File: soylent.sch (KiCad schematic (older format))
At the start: 21 parts, among them J1 DB9_Female, J2 Conn_01x04, J3 Conn_01x04, J4 Conn_02x03_Counter_Clockwise, Q1 BC847BPN, Q2 BC847BPN, U1 ATtiny202-SS, U2 MIC5504-3.3YM5

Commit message: Swap analog lines and reroute
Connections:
- net PA1: now also Q2.1 (E1), Q2.4 (E2), R5.1, R6.2
- net PA2: now also J4.1 (Pin_1); no longer Q2.1 (E1), Q2.4 (E2), R5.1, R6.2
- no-connect marks 8 -> 7
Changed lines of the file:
@@
 UPDI
-$Comp
-L Connector_Generic:Conn_02x03_Counter_Clockwise J4
-U 1 1 5DDE85A2
-P 6250 2800
-F 0 "J4" H 6300 3025 50  0000 C CNN
-F 1 "Conn_02x03_Counter_Clockwise" V 6345 2980 50  0001 L CNN
-F 2 "Pin_Headers:Pin_Header_Straight_2x03_Pitch2.54mm" H 6250 2800 50  0001 C CNN
-F 3 "~" H 6250 2800 50  0001 C CNN
-	1    6250 2800
-	1    0    0    1
-$EndComp
 $Comp
 L Transistor_BJT:BC847BPN Q1
@@
 	8250 4250 8250 2400
 Wire Wire Line
-	4000 3700 4400 3700
-Wire Wire Line
-	4400 3700 4400 3000
-Wire Wire Line
 	4400 3000 4600 3000
-Connection ~ 4000 3700
-NoConn ~ 6050 2900
 NoConn ~ 6050 2700
 NoConn ~ 6550 2700
 NoConn ~ 6550 2800
+$Comp
+L Connector_Generic:Conn_02x03_Counter_Clockwise J4
+U 1 1 5DDE85A2
+P 6250 2800
+F 0 "J4" H 6300 3025 50  0000 C CNN
+F 1 "Conn_02x03_Counter_Clockwise" V 6345 2980 50  0001 L CNN
+F 2 "Pin_Headers:Pin_Header_Straight_2x03_Pitch2.54mm" H 6250 2800 50  0001 C CNN
+F 3 "~" H 6250 2800 50  0001 C CNN
+	1    6250 2800
+	1    0    0    1
+$EndComp
+Wire Wire Line
+	3950 3600 4400 3600
+Connection ~ 3950 3600
+Wire Wire Line
+	4400 3600 4400 3000
+Wire Wire Line
+	4000 3700 6050 3700
+Wire Wire Line
+	6050 2900 6050 3700
+Connection ~ 4000 3700
 $EndSCHEMATC

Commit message: Insert a resistor on output
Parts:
- added R8: 100R, Resistors_SMD:R_0603_HandSoldering, symbol Device:R
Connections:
- net PA2: now also R8.2; no longer J4.1 (Pin_1)
- new net: J4.1 (Pin_1), R8.1
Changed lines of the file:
@@
 	4400 3600 4400 3000
 Wire Wire Line
-	4000 3700 6050 3700
+	4000 3700 5400 3700
 Wire Wire Line
 	6050 2900 6050 3700
 Connection ~ 4000 3700
+$Comp
+L Device:R R8
+U 1 1 5DFD8224
+P 5550 3700
+F 0 "R8" V 5343 3700 50  0000 C CNN
+F 1 "100R" V 5434 3700 50  0000 C CNN
+F 2 "Resistors_SMD:R_0603_HandSoldering" V 5480 3700 50  0001 C CNN
+F 3 "~" H 5550 3700 50  0001 C CNN
+	1    5550 3700
+	0    1    1    0
+$EndComp
+Wire Wire Line
+	5700 3700 6050 3700
 $EndSCHEMATC

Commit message: Switch to an RC filter
    http://sim.okawa-denshi.jp/en/CRtool.php

    fc = 4080.8959767153[Hz]
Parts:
- added C3: .1u, Capacitor_SMD:C_0603_1608Metric, symbol Device:C
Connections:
- net GND: now also C3.2
- net at J4.1 (Pin_1), R8.1: now also C3.1
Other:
- moved on the sheet: R8
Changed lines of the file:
@@
 Wire Wire Line
 	4400 3600 4400 3000
-Wire Wire Line
-	4000 3700 5400 3700
-Wire Wire Line
-	6050 2900 6050 3700
 Connection ~ 4000 3700
 $Comp
 L Device:R R8
 U 1 1 5DFD8224
-P 5550 3700
-F 0 "R8" V 5343 3700 50  0000 C CNN
-F 1 "100R" V 5434 3700 50  0000 C CNN
-F 2 "Resistors_SMD:R_0603_HandSoldering" V 5480 3700 50  0001 C CNN
-F 3 "~" H 5550 3700 50  0001 C CNN
-	1    5550 3700
+P 5700 3100
+F 0 "R8" V 5493 3100 50  0000 C CNN
+F 1 "100R" V 5584 3100 50  0000 C CNN
+F 2 "Resistors_SMD:R_0603_HandSoldering" V 5630 3100 50  0001 C CNN
+F 3 "~" H 5700 3100 50  0001 C CNN
+	1    5700 3100
 	0    1    1    0
 $EndComp
 Wire Wire Line
-	5700 3700 6050 3700
+	5450 3700 5450 3100
+Wire Wire Line
+	5450 3100 5550 3100
+Wire Wire Line
+	4000 3700 5450 3700
+$Comp
+L Device:C C3
+U 1 1 5DFEE336
+P 5950 3250
+F 0 "C3" H 6065 3296 50  0000 L CNN
+F 1 ".1u" H 6065 3205 50  0000 L CNN
+F 2 "Capacitor_SMD:C_0603_1608Metric" H 5988 3100 50  0001 C CNN
+F 3 "~" H 5950 3250 50  0001 C CNN
+	1    5950 3250
+	1    0    0    -1
+$EndComp
+$Comp
+L power:GND #PWR0111
+U 1 1 5DFEEE43
+P 5950 3400
+F 0 "#PWR0111" H 5950 3150 50  0001 C CNN
+F 1 "GND" H 5955 3227 50  0000 C CNN
+F 2 "" H 5950 3400 50  0001 C CNN
+F 3 "" H 5950 3400 50  0001 C CNN
+	1    5950 3400
+	1    0    0    -1
+$EndComp
+Wire Wire Line
+	5850 3100 5950 3100
+Wire Wire Line
+	5950 3100 6050 3100
+Wire Wire Line
+	6050 3100 6050 2900
+Connection ~ 5950 3100
 $EndSCHEMATC

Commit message: Use hand-soldering footprints more consistently
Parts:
- C1, C2, C3: footprint Capacitor_SMD:C_0603_1608Metric -> Capacitor_SMD:C_0603_1608Metric_Pad1.05x0.95mm_HandSolder
- D1, D2: footprint Diode_SMD:D_0603_1608Metric -> Diode_SMD:D_0603_1608Metric_Pad1.05x0.95mm_HandSolder
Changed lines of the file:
@@
 F 0 "C2" V 7048 5400 50  0000 C CNN
 F 1 "1u" V 7139 5400 50  0000 C CNN
-F 2 "Capacitor_SMD:C_0603_1608Metric" H 7338 5250 50  0001 C CNN
+F 2 "Capacitor_SMD:C_0603_1608Metric_Pad1.05x0.95mm_HandSolder" H 7338 5250 50  0001 C CNN
 F 3 "~" H 7300 5400 50  0001 C CNN
 	1    7300 5400
@@
 F 0 "C1" V 6748 5400 50  0000 C CNN
 F 1 "1u" V 6839 5400 50  0000 C CNN
-F 2 "Capacitor_SMD:C_0603_1608Metric" H 7038 5250 50  0001 C CNN
+F 2 "Capacitor_SMD:C_0603_1608Metric_Pad1.05x0.95mm_HandSolder" H 7038 5250 50  0001 C CNN
 F 3 "~" H 7000 5400 50  0001 C CNN
 	1    7000 5400
@@
 F 0 "D1" V 7946 4628 50  0000 L CNN
 F 1 "D" V 7855 4628 50  0000 L CNN
-F 2 "Diode_SMD:D_0603_1608Metric" H 7900 4550 50  0001 C CNN
+F 2 "Diode_SMD:D_0603_1608Metric_Pad1.05x0.95mm_HandSolder" H 7900 4550 50  0001 C CNN
 F 3 "~" H 7900 4550 50  0001 C CNN
 	1    7900 4550
@@
 F 0 "D2" V 8096 4571 50  0000 R CNN
 F 1 "D" V 8005 4571 50  0000 R CNN
-F 2 "Diode_SMD:D_0603_1608Metric" H 8050 4650 50  0001 C CNN
+F 2 "Diode_SMD:D_0603_1608Metric_Pad1.05x0.95mm_HandSolder" H 8050 4650 50  0001 C CNN
 F 3 "~" H 8050 4650 50  0001 C CNN
 	1    8050 4650
@@
 F 0 "C3" H 6065 3296 50  0000 L CNN
 F 1 ".1u" H 6065 3205 50  0000 L CNN
-F 2 "Capacitor_SMD:C_0603_1608Metric" H 5988 3100 50  0001 C CNN
+F 2 "Capacitor_SMD:C_0603_1608Metric_Pad1.05x0.95mm_HandSolder" H 5988 3100 50  0001 C CNN
 F 3 "~" H 5950 3250 50  0001 C CNN
 	1    5950 3250

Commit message: Rename pads
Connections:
- net PA1 renamed WIN
- net PA2 renamed WOUT
- net PA6 renamed TX
- net PA7 renamed RX
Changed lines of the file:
@@
 	7950 4800 8050 4800
 Text Label 3500 3600 0    50   ~ 0
-PA1
+WIN
 Text Label 3500 3700 0    50   ~ 0
-PA2
+WOUT
 Text Label 3500 3800 0    50   ~ 0
 PA3
 Text Label 3500 3900 0    50   ~ 0
-PA6
+TX
 Text Label 3500 4000 0    50   ~ 0
-PA7
+RX
 Wire Notes Line
 	8250 5750 6150 5750

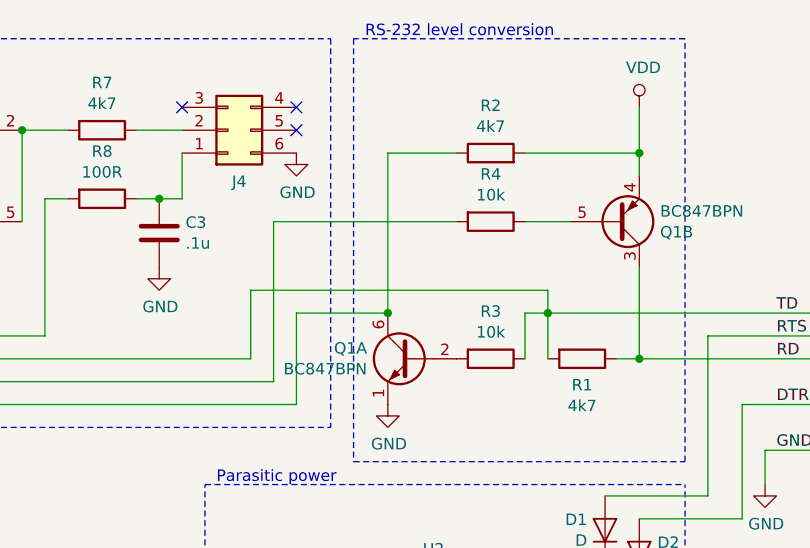
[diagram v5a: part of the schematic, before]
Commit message: Add a jumper for UPDI inhibit
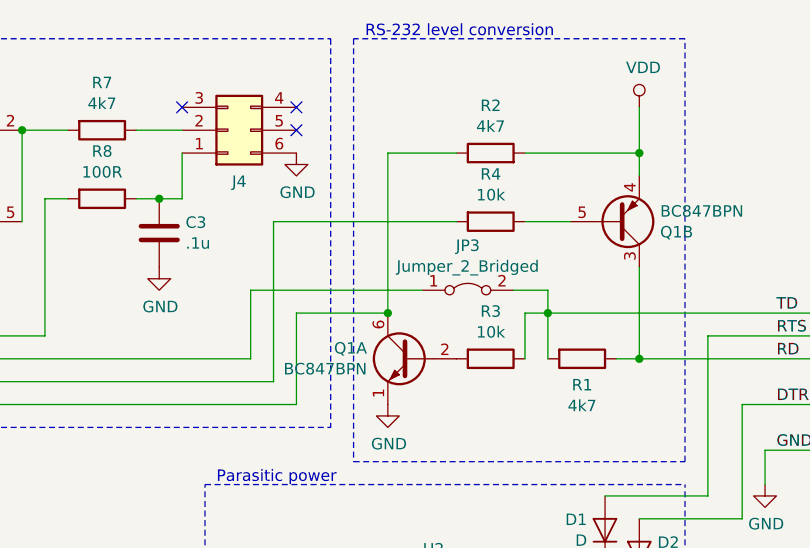
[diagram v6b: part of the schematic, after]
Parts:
- added JP3: Jumper_2_Bridged, Connector_PinHeader_2.54mm:PinHeader_2x01_P2.54mm_Vertical, symbol Jumper:Jumper_2_Bridged
- C1: footprint Capacitor_SMD:C_0603_1608Metric_Pad1.05x0.95mm_HandSolder -> Connector_PinHeader_2.54mm:PinHeader_1x02_P2.54mm_Vertical
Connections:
- net TD: now also JP3.2 (B); no longer J3.2 (Pin_2), U1.6 (~RESET~/PA0)
- new net UPDI: J3.2 (Pin_2), JP3.1 (A), U1.6 (~RESET~/PA0)
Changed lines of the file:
@@
 	7650 3500 7650 3600
 Connection ~ 7650 3600
-Wire Wire Line
-	7650 3600 7650 3800
 NoConn ~ 8900 4100
 NoConn ~ 8900 3400
@@
 F 0 "C1" V 6748 5400 50  0000 C CNN
 F 1 "1u" V 6839 5400 50  0000 C CNN
-F 2 "Capacitor_SMD:C_0603_1608Metric_Pad1.05x0.95mm_HandSolder" H 7038 5250 50  0001 C CNN
+F 2 "Connector_PinHeader_2.54mm:PinHeader_1x02_P2.54mm_Vertical" H 7038 5250 50  0001 C CNN
 F 3 "~" H 7000 5400 50  0001 C CNN
 	1    7000 5400
@@
 	6350 3800 6350 3500
 Wire Wire Line
-	6350 3500 7650 3500
+	6350 3500 7100 3500
 Connection ~ 3900 3500
 $Comp
@@
 	6050 3100 6050 2900
 Connection ~ 5950 3100
+Wire Wire Line
+	7500 3500 7650 3500
+$Comp
+L Jumper:Jumper_2_Bridged JP3
+U 1 1 5E09C5A1
+P 7300 3500
+F 0 "JP3" H 7300 3695 50  0000 C CNN
+F 1 "Jumper_2_Bridged" H 7300 3604 50  0000 C CNN
+F 2 "Connector_PinHeader_2.54mm:PinHeader_2x01_P2.54mm_Vertical" H 7300 3500 50  0001 C CNN
+F 3 "~" H 7300 3500 50  0001 C CNN
+	1    7300 3500
+	1    0    0    -1
+$EndComp
+Wire Wire Line
+	7650 3600 7650 3800
 $EndSCHEMATC

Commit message: Making more room on the schematic
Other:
- moved on the sheet: C3, J4, Q2A, Q2B, R5, R6, R7, R8
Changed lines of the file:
@@
 Connection ~ 3750 3900
 Wire Wire Line
-	6550 4000 6550 3600
-Wire Wire Line
-	6550 3600 6950 3600
+	6650 4000 6650 3600
+Wire Wire Line
+	6650 3600 6950 3600
 Connection ~ 3850 4000
 Wire Wire Line
@@
 Parasitic power
 Wire Notes Line
-	6700 2400 6700 4100
-Wire Notes Line
-	4250 4100 4250 2400
-Wire Wire Line
-	6450 3900 6450 3200
-Wire Wire Line
-	6450 3200 7250 3200
+	6700 1750 6700 3450
+Wire Notes Line
+	4250 3450 4250 1750
+Wire Wire Line
+	6750 3900 6750 3200
+Wire Wire Line
+	6750 3200 7250 3200
 Wire Wire Line
 	7550 3200 7750 3200
-Text Notes 4300 2400 0    50   ~ 0
+Text Notes 4300 1750 0    50   ~ 0
 TTY interface
 $Comp
 L power:GND #PWR0108
 U 1 1 5DEFD9EC
-P 6550 2900
-F 0 "#PWR0108" H 6550 2650 50  0001 C CNN
-F 1 "GND" H 6555 2727 50  0000 C CNN
-F 2 "" H 6550 2900 50  0001 C CNN
-F 3 "" H 6550 2900 50  0001 C CNN
-	1    6550 2900
+P 6600 2150
+F 0 "#PWR0108" H 6600 1900 50  0001 C CNN
+F 1 "GND" H 6605 1977 50  0000 C CNN
+F 2 "" H 6600 2150 50  0001 C CNN
+F 3 "" H 6600 2150 50  0001 C CNN
+	1    6600 2150
 	1    0    0    -1
 $EndComp
@@
 L Device:R R7
 U 1 1 5DEFDFE7
-P 5700 2800
-F 0 "R7" V 5493 2800 50  0000 C CNN
-F 1 "4k7" V 5584 2800 50  0000 C CNN
-F 2 "Resistors_SMD:R_0603_HandSoldering" V 5630 2800 50  0001 C CNN
-F 3 "~" H 5700 2800 50  0001 C CNN
-	1    5700 2800
-	0    1    1    0
+P 5700 2200
+F 0 "R7" V 5493 2200 50  0000 C CNN
+F 1 "4k7" V 5584 2200 50  0000 C CNN
+F 2 "Resistors_SMD:R_0603_HandSoldering" V 5630 2200 50  0001 C CNN
+F 3 "~" H 5700 2200 50  0001 C CNN
+	1    5700 2200
+	0    1    -1   0
 $EndComp
 $Comp
 L Transistor_BJT:BC847BPN Q2
 U 2 1 5DF05573
-P 5150 3200
-F 0 "Q2" H 5341 3154 50  0000 L CNN
-F 1 "BC847BPN" H 5341 3245 50  0000 L CNN
-F 2 "TO_SOT_Packages_SMD:SOT-363_SC-70-6_Handsoldering" H 5350 3300 50  0001 C CNN
-F 3 "https://assets.nexperia.com/documents/data-sheet/BC847BPN.pdf" H 5150 3200 50  0001 C CNN
-	2    5150 3200
+P 5150 2600
+F 0 "Q2" H 5341 2554 50  0000 L CNN
+F 1 "BC847BPN" H 5341 2645 50  0000 L CNN
+F 2 "TO_SOT_Packages_SMD:SOT-363_SC-70-6_Handsoldering" H 5350 2700 50  0001 C CNN
+F 3 "https://assets.nexperia.com/documents/data-sheet/BC847BPN.pdf" H 5150 2600 50  0001 C CNN
+	2    5150 2600
 	-1   0    0    1
 $EndComp
@@
 L Transistor_BJT:BC847BPN Q2
 U 1 1 5DF18897
-P 5150 2800
-F 0 "Q2" H 5341 2846 50  0000 L CNN
-F 1 "BC847BPN" H 5341 2755 50  0000 L CNN
-F 2 "TO_SOT_Packages_SMD:SOT-363_SC-70-6_Handsoldering" H 5350 2900 50  0001 C CNN
-F 3 "https://assets.nexperia.com/documents/data-sheet/BC847BPN.pdf" H 5150 2800 50  0001 C CNN
-	1    5150 2800
+P 5150 2200
+F 0 "Q2" H 5341 2246 50  0000 L CNN
+F 1 "BC847BPN" H 5341 2155 50  0000 L CNN
+F 2 "TO_SOT_Packages_SMD:SOT-363_SC-70-6_Handsoldering" H 5350 2300 50  0001 C CNN
+F 3 "https://assets.nexperia.com/documents/data-sheet/BC847BPN.pdf" H 5150 2200 50  0001 C CNN
+	1    5150 2200
 	-1   0    0    -1
 $EndComp
 Wire Wire Line
-	3750 3900 6450 3900
-Wire Wire Line
-	3850 4000 6550 4000
-Wire Notes Line
-	4250 2400 6700 2400
-Wire Notes Line
-	4250 4100 6700 4100
+	3750 3900 6750 3900
+Wire Wire Line
+	3850 4000 6650 4000
+Wire Notes Line
+	4250 1750 6700 1750
+Wire Notes Line
+	4250 3450 6700 3450
 Wire Wire Line
 	3900 3500 4100 3500
@@
 	4100 3500 4100 3800
 Wire Wire Line
-	4100 3800 6350 3800
-Wire Wire Line
-	6350 3800 6350 3500
-Wire Wire Line
-	6350 3500 7100 3500
+	4100 3800 6550 3800
+Wire Wire Line
+	6550 3800 6550 3500
+Wire Wire Line
+	6550 3500 7100 3500
 Connection ~ 3900 3500
 $Comp
 L power:VDD #PWR0109
 U 1 1 5DF48DE3
-P 5050 2600
-F 0 "#PWR0109" H 5050 2450 50  0001 C CNN
-F 1 "VDD" H 5068 2773 50  0000 C CNN
-F 2 "" H 5050 2600 50  0001 C CNN
-F 3 "" H 5050 2600 50  0001 C CNN
-	1    5050 2600
-	1    0    0    -1
-$EndComp
-$Comp
-L power:GND #PWR0110
-U 1 1 5DF492BB
-P 5050 3400
-F 0 "#PWR0110" H 5050 3150 50  0001 C CNN
-F 1 "GND" H 5055 3227 50  0000 C CNN
-F 2 "" H 5050 3400 50  0001 C CNN
-F 3 "" H 5050 3400 50  0001 C CNN
-	1    5050 3400
-	1    0    0    -1
-$EndComp
-Wire Wire Line
-	5050 3000 4600 3000
-Connection ~ 5050 3000
-Wire Wire Line
-	5350 3200 5350 2800
-Wire Wire Line
-	5350 2800 5550 2800
-Connection ~ 5350 2800
-Wire Wire Line
-	5850 2800 6050 2800
+P 5050 2000
+F 0 "#PWR0109" H 5050 1850 50  0001 C CNN
+F 1 "VDD" H 5068 2173 50  0000 C CNN
+F 2 "" H 5050 2000 50  0001 C CNN
+F 3 "" H 5050 2000 50  0001 C CNN
+	1    5050 2000
+	1    0    0    -1
+$EndComp
+Wire Wire Line
+	5050 2400 4600 2400
+Connection ~ 5050 2400
+Wire Wire Line
+	5350 2600 5350 2200
+Wire Wire Line
+	5350 2200 5550 2200
+Connection ~ 5350 2200
 $Comp
 L Device:R R5
 U 1 1 5DF5183F
-P 4600 2850
-F 0 "R5" H 4670 2804 50  0000 L CNN
-F 1 "10k" H 4670 2895 50  0000 L CNN
-F 2 "Resistors_SMD:R_0603_HandSoldering" V 4530 2850 50  0001 C CNN
-F 3 "~" H 4600 2850 50  0001 C CNN
-	1    4600 2850
+P 4600 2250
+F 0 "R5" H 4670 2204 50  0000 L CNN
+F 1 "10k" H 4670 2295 50  0000 L CNN
+F 2 "Resistors_SMD:R_0603_HandSoldering" V 4530 2250 50  0001 C CNN
+F 3 "~" H 4600 2250 50  0001 C CNN
+	1    4600 2250
 	-1   0    0    1
 $EndComp
@@
 L Device:R R6
 U 1 1 5DF52A36
-P 4600 3150
-F 0 "R6" H 4670 3104 50  0000 L CNN
-F 1 "10k" H 4670 3195 50  0000 L CNN
-F 2 "Resistors_SMD:R_0603_HandSoldering" V 4530 3150 50  0001 C CNN
-F 3 "~" H 4600 3150 50  0001 C CNN
-	1    4600 3150
+P 4600 2550
+F 0 "R6" H 4670 2504 50  0000 L CNN
+F 1 "10k" H 4670 2595 50  0000 L CNN
+F 2 "Resistors_SMD:R_0603_HandSoldering" V 4530 2550 50  0001 C CNN
+F 3 "~" H 4600 2550 50  0001 C CNN
+	1    4600 2550
 	-1   0    0    1
 $EndComp
-Connection ~ 4600 3000
-Wire Wire Line
-	5050 2600 4600 2600
-Wire Wire Line
-	4600 2600 4600 2700
-Connection ~ 5050 2600
-Wire Wire Line
-	5050 3400 4600 3400
-Wire Wire Line
-	4600 3400 4600 3300
-Connection ~ 5050 3400
+Connection ~ 4600 2400
+Wire Wire Line
+	5050 2000 4600 2000
+Wire Wire Line
+	4600 2000 4600 2100
+Connection ~ 5050 2000
+Wire Wire Line
+	5050 2800 4600 2800
+Wire Wire Line
+	4600 2800 4600 2700
 Wire Wire Line
 	8350 3700 8350 4400
@@
 	8250 4250 8250 2400
 Wire Wire Line
-	4400 3000 4600 3000
-NoConn ~ 6050 2700
-NoConn ~ 6550 2700
-NoConn ~ 6550 2800
+	4400 2400 4600 2400
+NoConn ~ 6100 1950
+NoConn ~ 6600 1950
+NoConn ~ 6600 2050
 $Comp
 L Connector_Generic:Conn_02x03_Counter_Clockwise J4
 U 1 1 5DDE85A2
-P 6250 2800
-F 0 "J4" H 6300 3025 50  0000 C CNN
-F 1 "Conn_02x03_Counter_Clockwise" V 6345 2980 50  0001 L CNN
-F 2 "Pin_Headers:Pin_Header_Straight_2x03_Pitch2.54mm" H 6250 2800 50  0001 C CNN
-F 3 "~" H 6250 2800 50  0001 C CNN
-	1    6250 2800
+P 6300 2050
+F 0 "J4" H 6350 2275 50  0000 C CNN
+F 1 "Conn_02x03_Counter_Clockwise" V 6395 2230 50  0001 L CNN
+F 2 "Pin_Headers:Pin_Header_Straight_2x03_Pitch2.54mm" H 6300 2050 50  0001 C CNN
+F 3 "~" H 6300 2050 50  0001 C CNN
+	1    6300 2050
 	1    0    0    1
 $EndComp
@@
 	3950 3600 4400 3600
 Connection ~ 3950 3600
-Wire Wire Line
-	4400 3600 4400 3000
 Connection ~ 4000 3700
 $Comp
 L Device:R R8
 U 1 1 5DFD8224
-P 5700 3100
-F 0 "R8" V 5493 3100 50  0000 C CNN
-F 1 "100R" V 5584 3100 50  0000 C CNN
-F 2 "Resistors_SMD:R_0603_HandSoldering" V 5630 3100 50  0001 C CNN
-F 3 "~" H 5700 3100 50  0001 C CNN
-	1    5700 3100
+P 5700 2900
+F 0 "R8" V 5493 2900 50  0000 C CNN
+F 1 "100R" V 5584 2900 50  0000 C CNN
+F 2 "Resistors_SMD:R_0603_HandSoldering" V 5630 2900 50  0001 C CNN
+F 3 "~" H 5700 2900 50  0001 C CNN
+	1    5700 2900
 	0    1    1    0
 $EndComp
-Wire Wire Line
-	5450 3700 5450 3100
-Wire Wire Line
-	5450 3100 5550 3100
-Wire Wire Line
-	4000 3700 5450 3700
 $Comp
 L Device:C C3
 U 1 1 5DFEE336
-P 5950 3250
-F 0 "C3" H 6065 3296 50  0000 L CNN
-F 1 ".1u" H 6065 3205 50  0000 L CNN
-F 2 "Capacitor_SMD:C_0603_1608Metric_Pad1.05x0.95mm_HandSolder" H 5988 3100 50  0001 C CNN
-F 3 "~" H 5950 3250 50  0001 C CNN
-	1    5950 3250
+P 5950 3050
+F 0 "C3" H 6065 3096 50  0000 L CNN
+F 1 ".1u" H 6065 3005 50  0000 L CNN
+F 2 "Capacitor_SMD:C_0603_1608Metric_Pad1.05x0.95mm_HandSolder" H 5988 2900 50  0001 C CNN
+F 3 "~" H 5950 3050 50  0001 C CNN
+	1    5950 3050
 	1    0    0    -1
 $EndComp
@@
 L power:GND #PWR0111
 U 1 1 5DFEEE43
-P 5950 3400
-F 0 "#PWR0111" H 5950 3150 50  0001 C CNN
-F 1 "GND" H 5955 3227 50  0000 C CNN
-F 2 "" H 5950 3400 50  0001 C CNN
-F 3 "" H 5950 3400 50  0001 C CNN
-	1    5950 3400
-	1    0    0    -1
-$EndComp
-Wire Wire Line
-	5850 3100 5950 3100
-Wire Wire Line
-	5950 3100 6050 3100
-Wire Wire Line
-	6050 3100 6050 2900
-Connection ~ 5950 3100
+P 5950 3200
+F 0 "#PWR0111" H 5950 2950 50  0001 C CNN
+F 1 "GND" H 5955 3027 50  0000 C CNN
+F 2 "" H 5950 3200 50  0001 C CNN
+F 3 "" H 5950 3200 50  0001 C CNN
+	1    5950 3200
+	1    0    0    -1
+$EndComp
+Wire Wire Line
+	5850 2900 5950 2900
 Wire Wire Line
 	7500 3500 7650 3500
@@
 Wire Wire Line
 	7650 3600 7650 3800
+Wire Wire Line
+	5850 2200 5950 2200
+Wire Wire Line
+	5950 2200 5950 2050
+Wire Wire Line
+	5950 2050 6100 2050
+Wire Wire Line
+	4400 2400 4400 3600
+Wire Wire Line
+	5950 2900 6050 2900
+Wire Wire Line
+	6050 2900 6050 2150
+Wire Wire Line
+	6050 2150 6100 2150
+Connection ~ 5950 2900
+Connection ~ 5050 2800
+$Comp
+L power:GND #PWR0110
+U 1 1 5DF492BB
+P 5050 2800
+F 0 "#PWR0110" H 5050 2550 50  0001 C CNN
+F 1 "GND" H 5055 2627 50  0000 C CNN
+F 2 "" H 5050 2800 50  0001 C CNN
+F 3 "" H 5050 2800 50  0001 C CNN
+	1    5050 2800
+	1    0    0    -1
+$EndComp
+Wire Wire Line
+	5450 2900 5550 2900
+Wire Wire Line
+	4000 3700 5450 3700
+Wire Wire Line
+	5450 3700 5450 2900
 $EndSCHEMATC
